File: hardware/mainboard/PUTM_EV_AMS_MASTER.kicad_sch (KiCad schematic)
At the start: 19 parts, among them J10 M300-MV10345M1, J4 FTSH-107-01-L-D-K, J5 M80-51004XX, J7 M300-MV10345M1, J8 M80-51004XX, T1 SM91502ALE

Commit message: chore: sync
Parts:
- added J1: Conn_02x10_Odd_Even, Connector_PinHeader_2.00mm:PinHeader_2x10_P2.00mm_Vertical, symbol Connector_Generic:Conn_02x10_Odd_Even
- added J2: Conn_02x03_Odd_Even, Connector_PinHeader_2.00mm:PinHeader_2x03_P2.00mm_Vertical, symbol Connector_Generic:Conn_02x03_Odd_Even
- added J3: Conn_02x04_Odd_Even, Connector_PinHeader_2.00mm:PinHeader_2x04_P2.00mm_Vertical, symbol Connector_Generic:Conn_02x04_Odd_Even
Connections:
- net +3.3VIO: now also J1.14 (Pin_14)
- net +5VIO: now also J1.16 (Pin_16)
- net AIR_M-: now also J2.1 (Pin_1)
- net AIR_M_DETECTION: now also J1.12 (Pin_12)
- net AIR_P-: now also J2.3 (Pin_3)
- net AIR_PRE-: now also J2.5 (Pin_5)
- net AIR_PRE_DETECTION: now also J1.10 (Pin_10)
- net AIR_P_DETECTION: now also J1.8 (Pin_8)
- net CHARGER_DETECTION: now also J1.6 (Pin_6)
- net D+: now also J1.3 (Pin_3)
- net D-: now also J1.1 (Pin_1)
- net ERROR_RELAY-: now also J1.17 (Pin_17)
- net EX_CANFD1_RX: now also J1.5 (Pin_5)
- net EX_CANFD1_TX: now also J1.7 (Pin_7)
- net EX_CANFD2_RX: now also J1.9 (Pin_9)
- net EX_CANFD2_TX: now also J1.11 (Pin_11)
- net FAN1-: now also J3.1 (Pin_1)
- net FAN2-: now also J3.3 (Pin_3)
- net FAN3-: now also J3.5 (Pin_5)
- net FAN4-: now also J3.7 (Pin_7)
- net GND: now also J1.2 (Pin_2), J1.20 (Pin_20)
- net TSMS_DETECTION: now also J1.13 (Pin_13)
- net VBUS+: now also J1.4 (Pin_4)
- net VDD: now also J1.19 (Pin_19)
- no-connect marks 13 -> 20
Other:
- removed sheet AIR Control
- removed sheet Fan Control
- note added: "AIR & FAN"
- note removed: "AIR"
- note removed: "FAN"
- note removed: "use cheaper connectors for ioslation pcb interface - 2mm spacing between pins"

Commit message: jenrzej colab
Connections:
- net VBUS+ is gone; now on net DETVUSB: J1.4 (Pin_4)
- net +5VA: now also J1.15 (Pin_15)
- net AIR_M_DETECTION: no longer J1.12 (Pin_12)
- net AIR_PRE_DETECTION: no longer J1.10 (Pin_10)
- net AIR_P_DETECTION: no longer J1.8 (Pin_8)
- net CHARGER_DETECTION: no longer J1.6 (Pin_6)
- net VDD renamed +3.3VA
- no-connect marks 20 -> 19
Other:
- removed sheet Power
- note added: "FTDI RST"
- note added: "UART NIE USB"

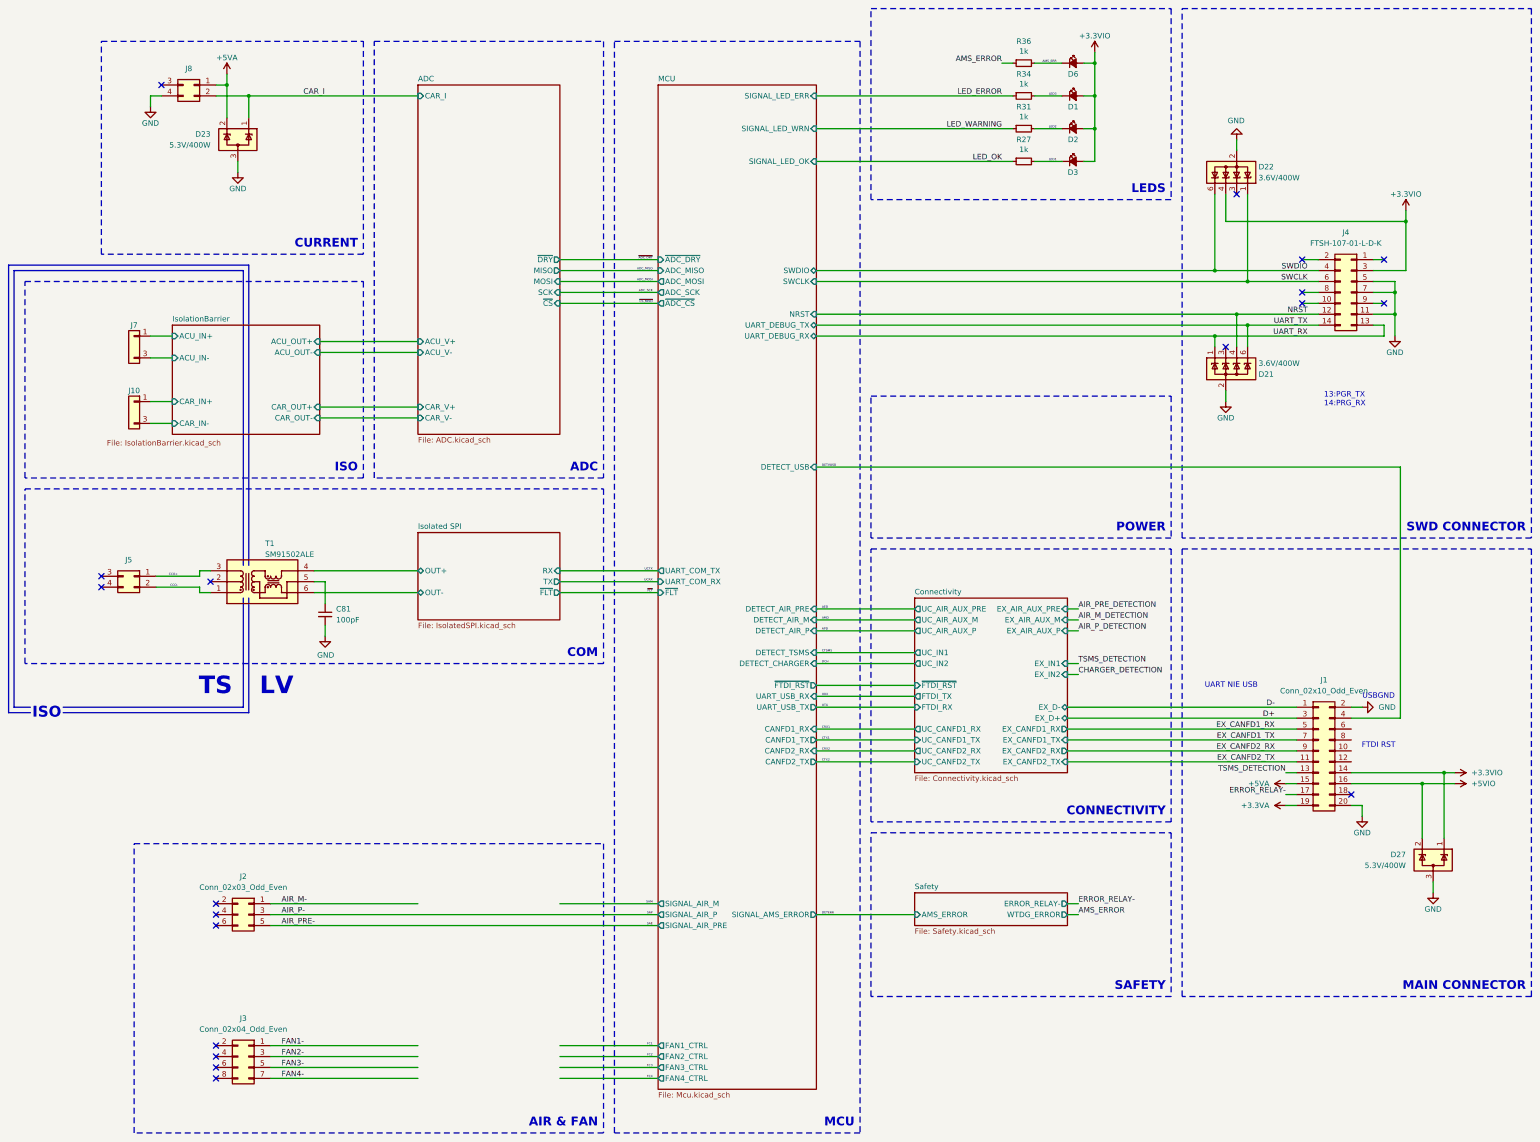
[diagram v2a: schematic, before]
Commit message: Cleaned up schematic, changed USB to UART, changed pinout of AIR sandwich connector
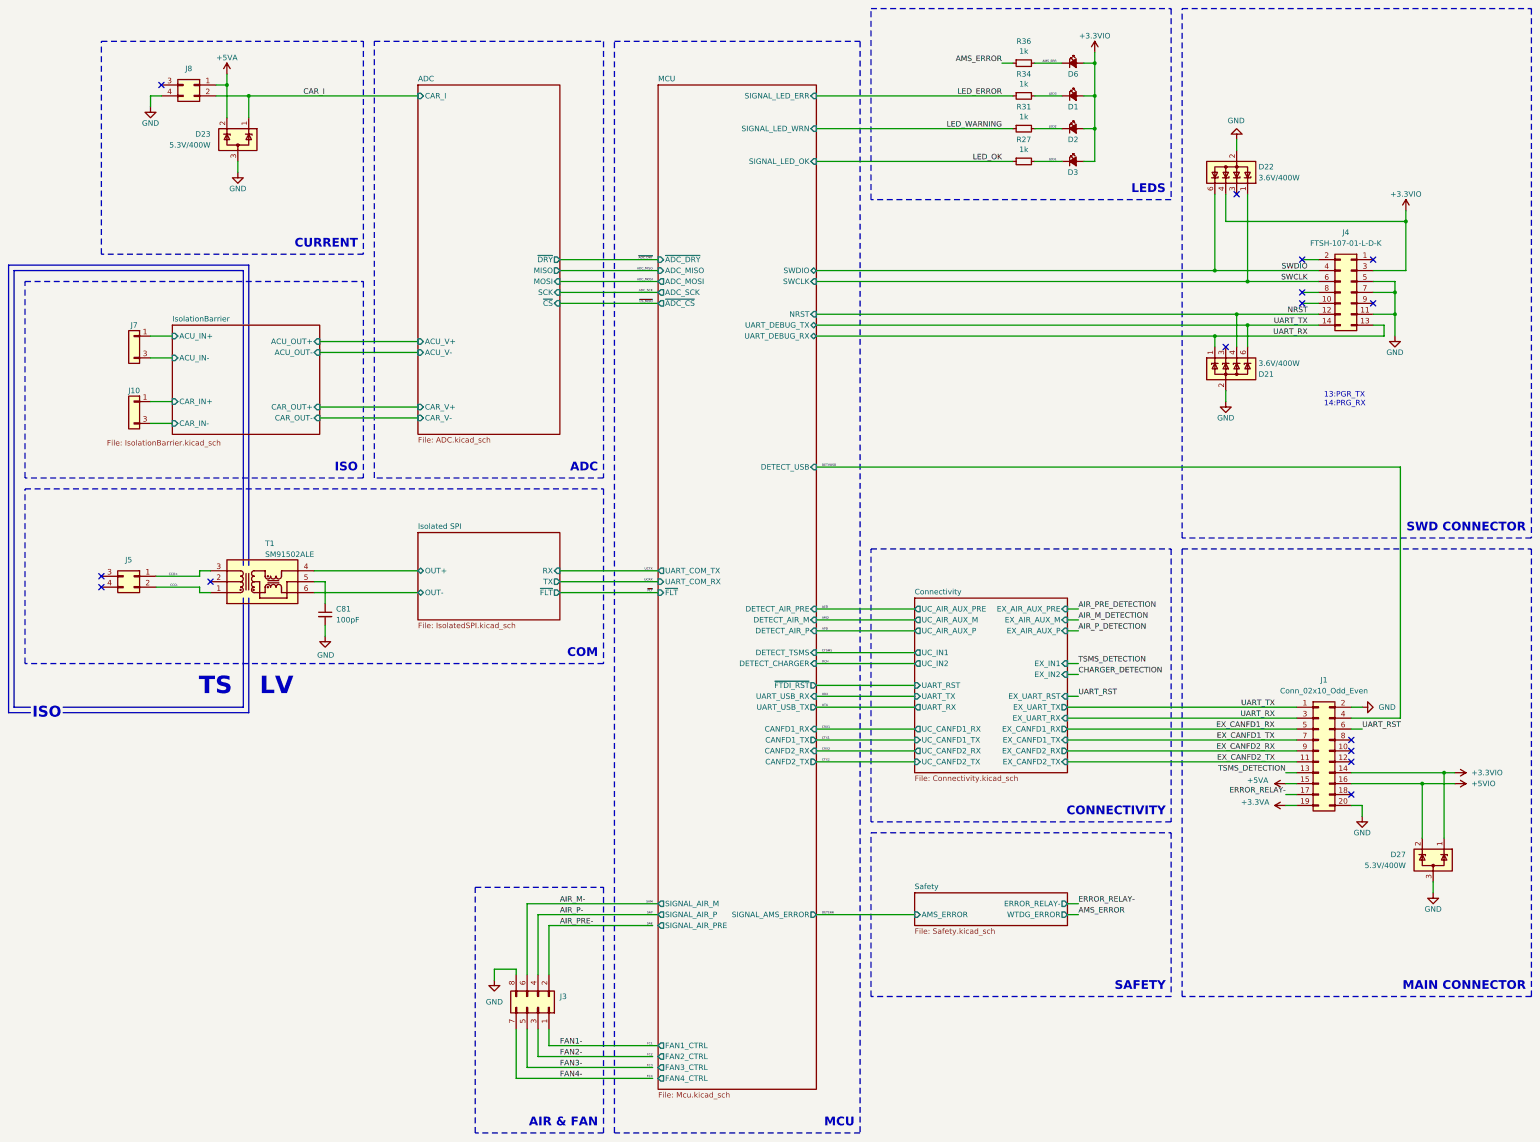
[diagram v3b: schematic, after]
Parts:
- removed J2: Conn_02x03_Odd_Even, Connector_PinHeader_2.00mm:PinHeader_2x03_P2.00mm_Vertical, symbol Connector_Generic:Conn_02x03_Odd_Even
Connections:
- net D+ is gone; now on net UART_RX: J1.3 (Pin_3)
- net D- is gone; now on net UART_TX: J1.1 (Pin_1)
- net AIR_M-: now also J3.6 (Pin_6)
- net AIR_P-: now also J3.4 (Pin_4)
- net AIR_PRE-: now also J3.2 (Pin_2)
- net GND: now also J3.8 (Pin_8)
- net UART_RST: now reaches J1.6 (Pin_6)
- no-connect marks 19 -> 15
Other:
- sheet Connectivity ports: added EX_UART_RST, EX_UART_RX, EX_UART_TX, UART_RST, UART_RX, UART_TX; removed EX_D+, EX_D-, FTDI_RX, FTDI_TX, ~{FTDI_RST}
- note removed: "FTDI RST"
- note removed: "POWER"
- note removed: "UART NIE USB"
- note removed: "USBGND"
- moved on the sheet: J3

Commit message: Routed AIR detection signal to main connector
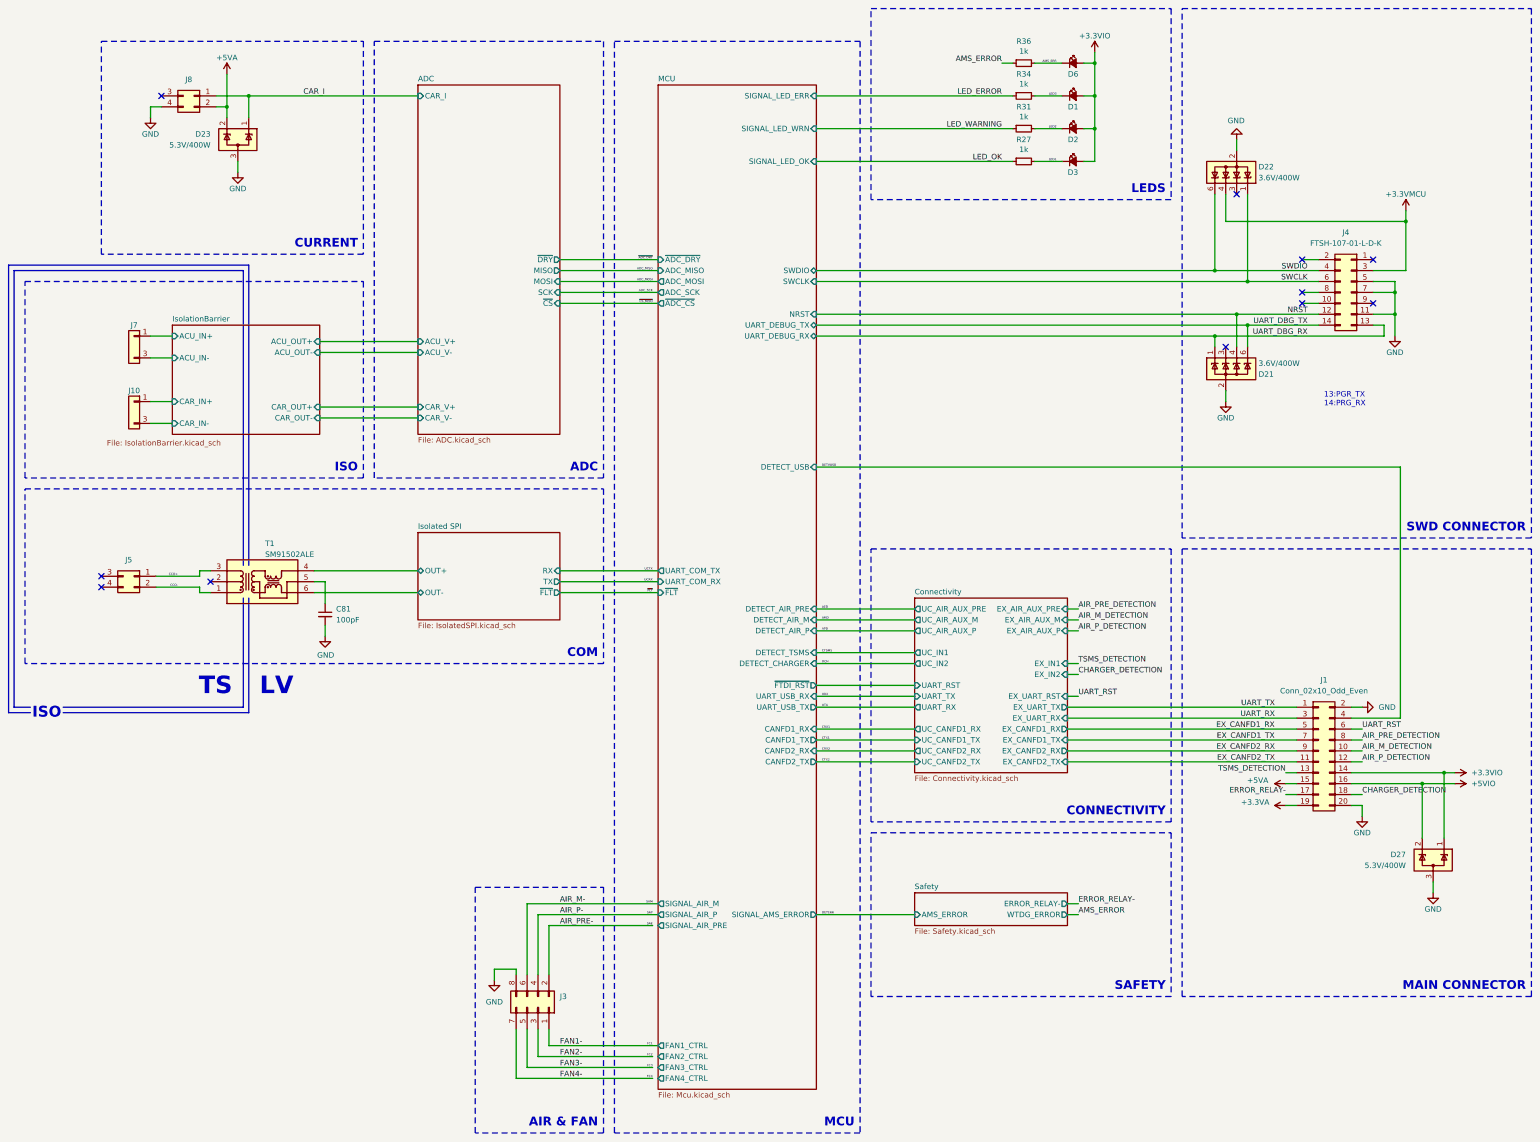
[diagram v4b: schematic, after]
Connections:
- net +3.3VIO: no longer D22.4 (A), J4.3 (Pin_3)
- net +5VA: now also J8.2 (Pin_2); no longer J8.1 (Pin_1)
- net AIR_M_DETECTION: now also J1.10 (Pin_10)
- net AIR_PRE_DETECTION: now also J1.8 (Pin_8)
- net AIR_P_DETECTION: now also J1.12 (Pin_12)
- net CAR_I: now also J8.1 (Pin_1); no longer J8.2 (Pin_2)
- net CHARGER_DETECTION: now also J1.18 (Pin_18)
- net UART_RX: no longer D21.1 (A), J4.13 (Pin_13)
- net UART_TX: no longer D21.6 (A), J4.14 (Pin_14)
- new net +3.3VMCU: D22.4 (A), J4.3 (Pin_3)
- new net UART_DBG_RX: D21.1 (A), J4.13 (Pin_13)
- new net UART_DBG_TX: D21.6 (A), J4.14 (Pin_14)
- no-connect marks 15 -> 11
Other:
- moved on the sheet: J8
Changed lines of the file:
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@@
 	)
 	(junction
-		(at 83.82 35.56)
+		(at 83.82 40.64)
 		(diameter 0)
 		(color 0 0 0 0)
@@
 	)
 	(junction
+		(at 88.9 38.1)
+		(diameter 0)
+		(color 0 0 0 0)
+	)
+	(junction
 		(at 313.69 78.74)
 		(diameter 0)
@@
 	)
 	(junction
-		(at 88.9 38.1)
-		(diameter 0)
-		(color 0 0 0 0)
-	)
-	(junction
 		(at 321.31 91.44)
 		(diameter 0)
@@
 	)
 	(no_connect
-		(at 345.44 190.5)
-	)
-	(no_connect
-		(at 345.44 200.66)
-	)
-	(no_connect
 		(at 334.01 83.82)
 	)
 	(no_connect
-		(at 345.44 193.04)
-	)
-	(no_connect
 		(at 80.01 151.13)
 	)
@@
 	)
 	(no_connect
-		(at 68.58 35.56)
-	)
-	(no_connect
-		(at 345.44 187.96)
+		(at 68.58 38.1)
 	)
 	(no_connect
@@
 	(wire
 		(pts
+			(xy 345.44 190.5) (xy 347.98 190.5)
+		)
+		(stroke
+			(width 0)
+			(type default)
+		)
+	)
+	(wire
+		(pts
 			(xy 220.98 78.74) (xy 313.69 78.74)
 		)
@@
 	(wire
 		(pts
-			(xy 220.98 175.26) (xy 243.84 175.26)
+			(xy 345.44 193.04) (xy 347.98 193.04)
 		)
 		(stroke
@@
 	(wire
 		(pts
-			(xy 83.82 35.56) (xy 81.28 35.56)
+			(xy 220.98 175.26) (xy 243.84 175.26)
 		)
 		(stroke
@@
 	(wire
 		(pts
-			(xy 83.82 33.02) (xy 83.82 35.56)
+			(xy 83.82 33.02) (xy 83.82 40.64)
 		)
 		(stroke
@@
 	(wire
 		(pts
+			(xy 345.44 187.96) (xy 347.98 187.96)
+		)
+		(stroke
+			(width 0)
+			(type default)
+		)
+	)
+	(wire
+		(pts
 			(xy 77.47 153.67) (xy 80.01 153.67)
 		)
@@
 	(wire
 		(pts
-			(xy 66.04 38.1) (xy 66.04 40.64)
+			(xy 345.44 200.66) (xy 347.98 200.66)
+		)
+		(stroke
+			(width 0)
+			(type default)
+		)
+	)
+	(wire
+		(pts
+			(xy 66.04 40.64) (xy 66.04 43.18)
 		)
 		(stroke
@@
 	(wire
 		(pts
+			(xy 81.28 38.1) (xy 88.9 38.1)
+		)
+		(stroke
+			(width 0)
+			(type default)
+		)
+	)
+	(wire
+		(pts
 			(xy 347.98 203.2) (xy 347.98 205.74)
 		)
@@
 	(wire
 		(pts
+			(xy 81.28 40.64) (xy 83.82 40.64)
+		)
+		(stroke
+			(width 0)
+			(type default)
+		)
+	)
+	(wire
+		(pts
 			(xy 350.52 81.28) (xy 355.6 81.28)
 		)
@@
 	(wire
 		(pts
-			(xy 81.28 38.1) (xy 88.9 38.1)
-		)
-		(stroke
-			(width 0)
-			(type default)
-		)
-	)
-	(wire
-		(pts
 			(xy 367.03 195.58) (xy 367.03 210.82)
 		)
@@
 	(wire
 		(pts
-			(xy 83.82 35.56) (xy 83.82 43.18)
-		)
-		(stroke
-			(width 0)
-			(type default)
-		)
-	)
-	(wire
-		(pts
 			(xy 182.88 261.62) (xy 156.21 261.62)
 		)
@@
 	(wire
 		(pts
+			(xy 83.82 40.64) (xy 83.82 43.18)
+		)
+		(stroke
+			(width 0)
+			(type default)
+		)
+	)
+	(wire
+		(pts
 			(xy 278.13 53.34) (xy 271.78 53.34)
 		)
@@
 	(wire
 		(pts
-			(xy 68.58 38.1) (xy 66.04 38.1)
+			(xy 68.58 40.64) (xy 66.04 40.64)
 		)
 		(stroke
@@
 		)
 	)
-	(label "UART_TX"
+	(label "UART_DBG_TX"
 		(at 335.28 91.44 180)
 		(effects
@@
 		)
 	)
-	(label "UART_RX"
+	(label "UART_DBG_RX"
 		(at 335.28 93.98 180)
 		(effects
@@
 		)
 	)
+	(label "AIR_PRE_DETECTION"
+		(at 347.98 187.96 0)
+		(effects
+			(font
+				(size 1.27 1.27)
+			)
+			(justify left bottom)
+		)
+	)
 	(label "EX_CANFD2_TX"
 		(at 327.66 193.04 180)
@@
 		)
 	)
+	(label "CHARGER_DETECTION"
+		(at 347.98 200.66 0)
+		(effects
+			(font
+				(size 1.27 1.27)
+			)
+			(justify left bottom)
+		)
+	)
 	(label "AMD"
 		(at 222.25 160.02 0)
@@
 		)
 	)
+	(label "AIR_P_DETECTION"
+		(at 347.98 193.04 0)
+		(effects
+			(font
+				(size 1.27 1.27)
+			)
+			(justify left bottom)
+		)
+	)
 	(label "DCH"
 		(at 222.25 170.18 0)
@@
 		)
 	)
+	(label "AIR_M_DETECTION"
+		(at 347.98 190.5 0)
+		(effects
+			(font
+				(size 1.27 1.27)
+			)
+			(justify left bottom)
+		)
+	)
 	(label "EX_CANFD1_TX"
 		(at 327.6066 187.96 180)
@@
 	(symbol
 		(lib_id "Samacsys_kicad_sym:M80-51004XX")
-		(at 74.93 36.83 0)
+		(at 74.93 39.37 0)
 		(mirror y)
 		(unit 1)
@@
 		(fields_autoplaced yes)
 		(property "Reference" "J8"
-			(at 74.93 31.75 0)
+			(at 74.93 34.29 0)
 			(effects
 				(font
@@
 		)
 		(property "Value" "M80-51004XX"
-			(at 74.93 31.75 0)
+			(at 74.93 34.29 0)
 			(effects
 				(font
@@
 		)
 		(property "Footprint" "Samacsys:M80-51004YY"
-			(at 58.42 131.75 0)
+			(at 58.42 134.29 0)
 			(effects
 				(font
@@
 		)
 		(property "Datasheet" "https://cdn.harwin.com/pdfs/M80-510.pdf"
-			(at 58.42 231.75 0)
+			(at 58.42 234.29 0)
 			(effects
 				(font
@@
 		)
 		(property "Description" "4 Male DIL Vertical Throughboard Conn. Jackscrews, 2.00mm Pitch High-Reliability Connector - Datamate J-Tek"
-			(at 74.93 36.83 0)
+			(at 74.93 39.37 0)
 			(effects
 				(font
@@
 		)
 		(property "Height" ""
-			(at 58.42 431.75 0)
+			(at 58.42 434.29 0)
 			(effects
 				(font
@@
 		)
 		(property "Mouser Part Number" "855-M80-5100422"
-			(at 58.42 531.75 0)
+			(at 58.42 534.29 0)
 			(effects
 				(font
@@
 		)
 		(property "Mouser Price/Stock" "https://www.mouser.co.uk/ProductDetail/Harwin/M80-5100442?qs=wuXwK9wHm9vlrUDxU70C1Q%3D%3D"
-			(at 58.42 631.75 0)
+			(at 58.42 634.29 0)
 			(effects
 				(font
@@
 		)
 		(property "Manufacturer_Name" "Harwin"
-			(at 58.42 731.75 0)
+			(at 58.42 734.29 0)
 			(effects
 				(font
@@
 		)
 		(property "Manufacturer_Part_Number" "M80-5100442"
-			(at 58.42 831.75 0)
+			(at 58.42 834.29 0)
 			(effects
 				(font
@@
 		)
 		(property "Arrow Part Number" ""
-			(at 74.93 36.83 0)
+			(at 74.93 39.37 0)
 			(effects
 				(font
@@
 		)
 		(property "Arrow Price/Stock" ""
-			(at 74.93 36.83 0)
+			(at 74.93 39.37 0)
 			(effects
 				(font
@@
 		)
 		(property "DigiKey Part Number" ""
-			(at 74.93 36.83 0)
+			(at 74.93 39.37 0)
 			(effects
 				(font
@@
 		(lib_name "GND_7")
 		(lib_id "power:GND")
-		(at 66.04 40.64 0)
+		(at 66.04 43.18 0)
 		(unit 1)
 		(exclude_from_sim no)
@@
 		(dnp no)
 		(property "Reference" "#PWR0176"
-			(at 66.04 46.99 0)
+			(at 66.04 49.53 0)
 			(effects
 				(font
@@
 		)
 		(property "Value" "GND"
-			(at 66.04 44.45 0)
+			(at 66.04 46.99 0)
 			(effects
 				(font
@@
 		)
 		(property "Footprint" ""
-			(at 66.04 40.64 0)
+			(at 66.04 43.18 0)
 			(effects
 				(font
@@
 		)
 		(property "Datasheet" ""
-			(at 66.04 40.64 0)
+			(at 66.04 43.18 0)
 			(effects
 				(font
@@
 		)
 		(property "Description" ""
-			(at 66.04 40.64 0)
+			(at 66.04 43.18 0)
 			(effects
 				(font
@@
 	)
 	(symbol
+		(lib_name "+3.3V_1")
 		(lib_id "power:+3.3V")
 		(at 358.14 64.77 0)
@@
 		(on_board yes)
 		(dnp no)
-		(property "Reference" "#PWR073"
+		(property "Reference" "#PWR03"
 			(at 358.14 68.58 0)
 			(effects
@@
 			)
 		)
-		(property "Value" "+3.3VIO"
+		(property "Value" "+3.3VMCU"
 			(at 358.14 60.96 0)
 			(effects
@@
 			)
 		)
-		(property "Description" ""
+		(property "Description" "Power symbol creates a global label with name \"+3.3V\""
 			(at 358.14 64.77 0)
 			(effects
@@
 		)
 		(instances
-			(project "PUTM_EV_AMS_MASTER_2025"
+			(project "PUTM_EV_AMS_MASTER"
 				(path "/b456cffc-d9d7-4c91-91f2-36ec9a65dd1b"
-					(reference "#PWR073")
+					(reference "#PWR03")
 					(unit 1)
 				)
